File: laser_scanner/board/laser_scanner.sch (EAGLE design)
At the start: 31 parts

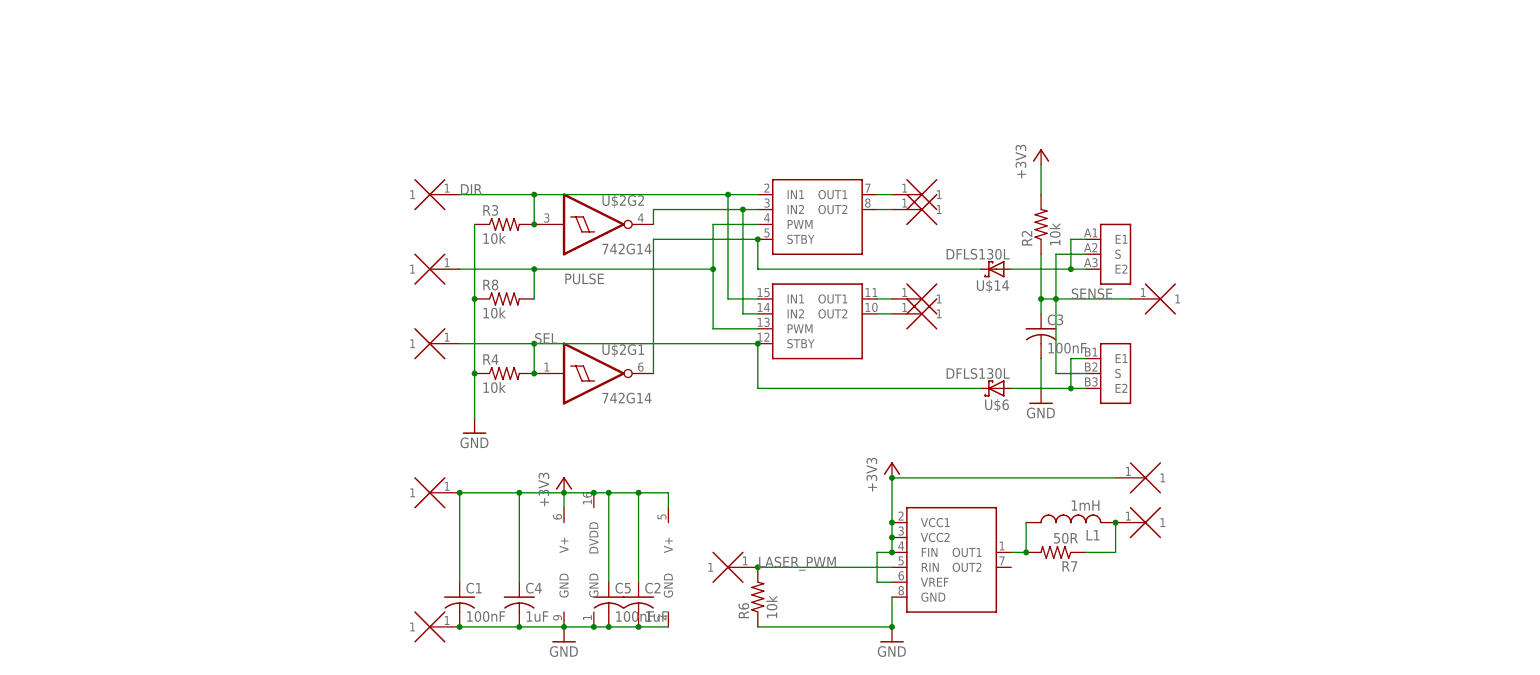
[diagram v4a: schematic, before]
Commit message: Made laser scanner more readable.
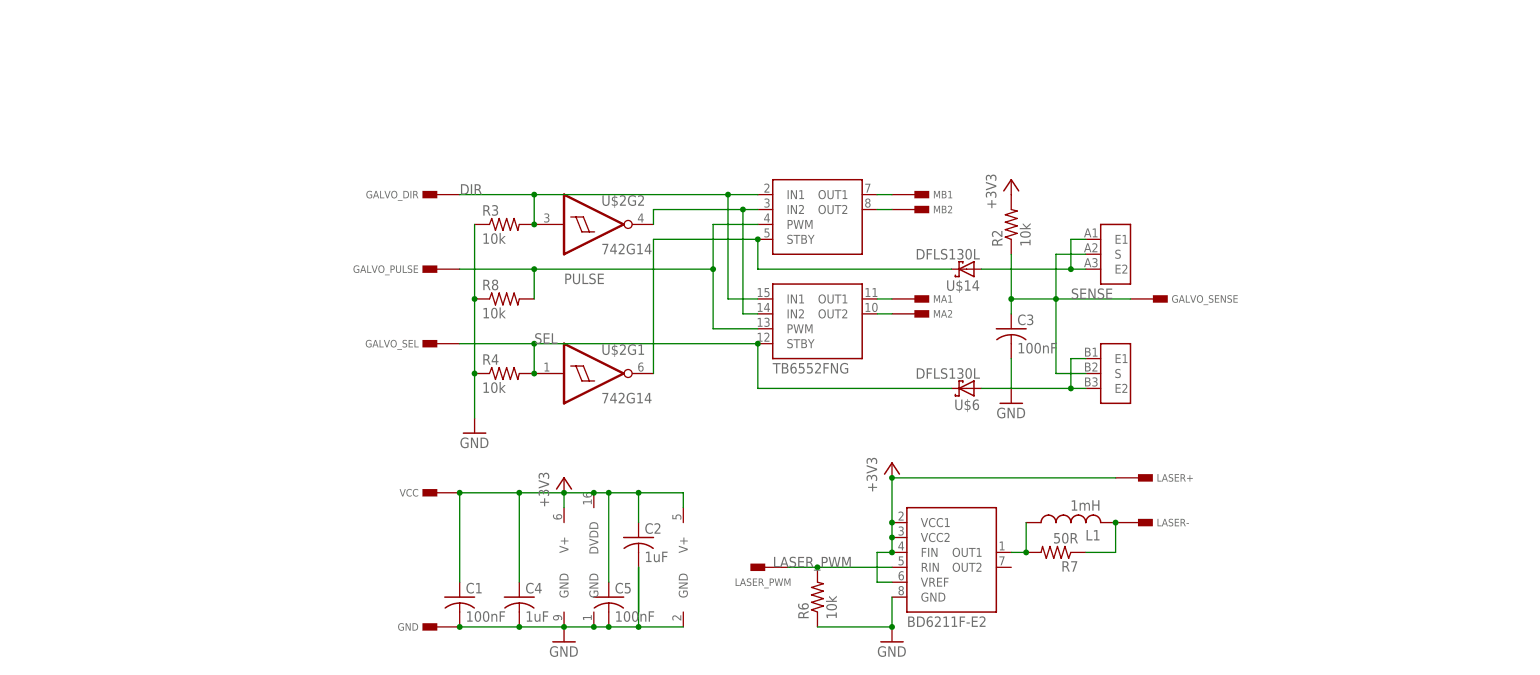
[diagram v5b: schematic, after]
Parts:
- renumbered L+ to LASER+, L- to LASER-
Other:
- note added: "BD6211F-E2"
- note added: "TB6552FNG"
- moved on the sheet: C2, C3, R2, R6, U$14, U$6
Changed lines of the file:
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@@
 <part name="R7" library="rcl" deviceset="R-US_" device="R0603" value="50R"/>
 <part name="LASER_PWM" library="modular_robotics" deviceset="PAD" device="-0.6_1.8"/>
-<part name="L-" library="modular_robotics" deviceset="PAD" device="-0.6_1.8"/>
+<part name="LASER-" library="modular_robotics" deviceset="PAD" device="-0.6_1.8"/>
 <part name="U$3" library="modular_robotics" deviceset="BD6211" device=""/>
 <part name="GND5" library="supply1" deviceset="GND" device=""/>
 <part name="+3V5" library="supply1" deviceset="+3V3" device=""/>
-<part name="L+" library="modular_robotics" deviceset="PAD" device="-0.6_1.8"/>
+<part name="LASER+" library="modular_robotics" deviceset="PAD" device="-0.6_1.8"/>
 <part name="R8" library="rcl" deviceset="R-US_" device="R0603" value="10k"/>
 <part name="U$2" library="modular_robotics" deviceset="74*2G14" device=""/>
@@
 <sheet>
 <plain>
+<text x="137.16" y="-15.24" size="1.778" layer="95">BD6211F-E2</text>
+<text x="114.3" y="27.94" size="1.778" layer="95">TB6552FNG</text>
 </plain>
 <instances>
@@
 <instance part="MA2" gate="G$1" x="139.7" y="38.1"/>
 <instance part="C1" gate="G$1" x="60.96" y="-10.16"/>
-<instance part="C2" gate="G$1" x="91.44" y="-10.16"/>
-<instance part="U$6" gate="G$1" x="152.4" y="25.4" rot="R180"/>
-<instance part="R2" gate="G$1" x="160.02" y="53.34" rot="R90"/>
+<instance part="C2" gate="G$1" x="91.44" y="0"/>
+<instance part="U$6" gate="G$1" x="147.32" y="25.4" rot="R180"/>
+<instance part="R2" gate="G$1" x="154.94" y="53.34" rot="R90"/>
 <instance part="U$7" gate="A" x="170.18" y="48.26"/>
 <instance part="U$7" gate="B" x="170.18" y="27.94"/>
@@
 <instance part="GND2" gate="1" x="63.5" y="17.78"/>
 <instance part="R4" gate="G$1" x="68.58" y="27.94"/>
-<instance part="C3" gate="G$1" x="160.02" y="35.56"/>
-<instance part="U$14" gate="G$1" x="152.4" y="45.72" rot="R180"/>
-<instance part="+3V3" gate="G$1" x="160.02" y="66.04"/>
-<instance part="GND3" gate="1" x="160.02" y="22.86"/>
+<instance part="C3" gate="G$1" x="154.94" y="35.56"/>
+<instance part="U$14" gate="G$1" x="147.32" y="45.72" rot="R180"/>
+<instance part="+3V3" gate="G$1" x="154.94" y="60.96"/>
+<instance part="GND3" gate="1" x="154.94" y="22.86"/>
 <instance part="L1" gate="G$1" x="165.1" y="2.54" rot="R90"/>
-<instance part="R6" gate="G$1" x="111.76" y="-10.16" rot="R90"/>
+<instance part="R6" gate="G$1" x="121.92" y="-10.16" rot="R90"/>
 <instance part="R7" gate="G$1" x="162.56" y="-2.54" rot="R180"/>
-<instance part="LASER_PWM" gate="G$1" x="106.68" y="-5.08" rot="R180"/>
-<instance part="L-" gate="G$1" x="177.8" y="2.54"/>
+<instance part="LASER_PWM" gate="G$1" x="111.76" y="-5.08" smashed="yes" rot="R180">
+<attribute name="NAME" x="117.475" y="-6.985" size="1.27" layer="95" rot="R180"/>
+</instance>
+<instance part="LASER-" gate="G$1" x="177.8" y="2.54"/>
 <instance part="U$3" gate="G$1" x="137.16" y="-12.7"/>
 <instance part="GND5" gate="1" x="134.62" y="-17.78"/>
 <instance part="+3V5" gate="G$1" x="134.62" y="12.7"/>
-<instance part="L+" gate="G$1" x="177.8" y="10.16"/>
+<instance part="LASER+" gate="G$1" x="177.8" y="10.16"/>
 <instance part="R8" gate="G$1" x="68.58" y="40.64"/>
-<instance part="U$2" gate="PWR" x="96.52" y="-5.08"/>
+<instance part="U$2" gate="PWR" x="99.06" y="-5.08"/>
 <instance part="U$2" gate="G2" x="83.82" y="53.34"/>
 <instance part="U$2" gate="G1" x="83.82" y="27.94"/>
@@
 <pinref part="U$2" gate="PWR" pin="GND"/>
 <wire x1="86.36" y1="-15.24" x2="91.44" y2="-15.24" width="0.1524" layer="91"/>
-<wire x1="96.52" y1="-15.24" x2="91.44" y2="-15.24" width="0.1524" layer="91"/>
-<junction x="91.44" y="-15.24"/>
+<wire x1="91.44" y1="-12.7" x2="91.44" y2="-5.08" width="0.1524" layer="91"/>
+<wire x1="99.06" y1="-15.24" x2="91.44" y2="-15.24" width="0.1524" layer="91"/>
+<wire x1="91.44" y1="-15.24" x2="91.44" y2="-5.08" width="0.1524" layer="91"/>
 <pinref part="C4" gate="G$1" pin="2"/>
 <junction x="71.12" y="-15.24"/>
 <pinref part="C5" gate="G$1" pin="2"/>
 <junction x="86.36" y="-15.24"/>
+<junction x="91.44" y="-15.24"/>
 </segment>
 <segment>
@@
 <pinref part="GND3" gate="1" pin="GND"/>
 <pinref part="C3" gate="G$1" pin="2"/>
-<wire x1="160.02" y1="25.4" x2="160.02" y2="30.48" width="0.1524" layer="91"/>
+<wire x1="154.94" y1="25.4" x2="154.94" y2="30.48" width="0.1524" layer="91"/>
 </segment>
 <segment>
@@
 <pinref part="U$3" gate="G$1" pin="GND"/>
 <pinref part="R6" gate="G$1" pin="1"/>
-<wire x1="134.62" y1="-15.24" x2="111.76" y2="-15.24" width="0.1524" layer="91"/>
+<wire x1="134.62" y1="-15.24" x2="121.92" y2="-15.24" width="0.1524" layer="91"/>
 <junction x="134.62" y="-15.24"/>
 <wire x1="134.62" y1="-10.16" x2="134.62" y2="-15.24" width="0.1524" layer="91"/>
@@
 <wire x1="60.96" y1="7.62" x2="60.96" y2="-7.62" width="0.1524" layer="91"/>
 <pinref part="C2" gate="G$1" pin="1"/>
-<wire x1="91.44" y1="-7.62" x2="91.44" y2="7.62" width="0.1524" layer="91"/>
+<wire x1="91.44" y1="2.54" x2="91.44" y2="7.62" width="0.1524" layer="91"/>
 <pinref part="U$1" gate="DPWR" pin="DVDD"/>
 <wire x1="91.44" y1="7.62" x2="86.36" y2="7.62" width="0.1524" layer="91"/>
@@
 <junction x="60.96" y="7.62"/>
 <pinref part="U$2" gate="PWR" pin="V+"/>
-<wire x1="96.52" y1="5.08" x2="96.52" y2="7.62" width="0.1524" layer="91"/>
-<wire x1="96.52" y1="7.62" x2="91.44" y2="7.62" width="0.1524" layer="91"/>
+<wire x1="99.06" y1="5.08" x2="99.06" y2="7.62" width="0.1524" layer="91"/>
+<wire x1="99.06" y1="7.62" x2="91.44" y2="7.62" width="0.1524" layer="91"/>
 <junction x="91.44" y="7.62"/>
 <pinref part="C4" gate="G$1" pin="1"/>
@@
 <pinref part="R2" gate="G$1" pin="2"/>
 <pinref part="+3V3" gate="G$1" pin="+3V3"/>
-<wire x1="160.02" y1="58.42" x2="160.02" y2="63.5" width="0.1524" layer="91"/>
-</segment>
-<segment>
-<pinref part="L+" gate="G$1" pin="1"/>
+</segment>
+<segment>
+<pinref part="LASER+" gate="G$1" pin="1"/>
 <wire x1="172.72" y1="10.16" x2="134.62" y2="10.16" width="0.1524" layer="91"/>
 <pinref part="U$3" gate="G$1" pin="VCC2"/>
@@
 <wire x1="60.96" y1="33.02" x2="73.66" y2="33.02" width="0.1524" layer="91"/>
 <wire x1="73.66" y1="33.02" x2="111.76" y2="33.02" width="0.1524" layer="91"/>
-<wire x1="149.86" y1="25.4" x2="111.76" y2="25.4" width="0.1524" layer="91"/>
+<wire x1="144.78" y1="25.4" x2="111.76" y2="25.4" width="0.1524" layer="91"/>
 <wire x1="111.76" y1="25.4" x2="111.76" y2="33.02" width="0.1524" layer="91"/>
 <junction x="111.76" y="33.02"/>
@@
 <pinref part="U$14" gate="G$1" pin="A"/>
 <pinref part="U$7" gate="A" pin="E2"/>
-<wire x1="154.94" y1="45.72" x2="165.1" y2="45.72" width="0.1524" layer="91"/>
+<wire x1="149.86" y1="45.72" x2="165.1" y2="45.72" width="0.1524" layer="91"/>
 <pinref part="U$7" gate="A" pin="E1"/>
 <wire x1="165.1" y1="45.72" x2="167.64" y2="45.72" width="0.1524" layer="91"/>
@@
 <wire x1="165.1" y1="25.4" x2="167.64" y2="25.4" width="0.1524" layer="91"/>
 <pinref part="U$6" gate="G$1" pin="A"/>
-<wire x1="165.1" y1="25.4" x2="154.94" y2="25.4" width="0.1524" layer="91"/>
+<wire x1="165.1" y1="25.4" x2="149.86" y2="25.4" width="0.1524" layer="91"/>
 <junction x="165.1" y="25.4"/>
 </segment>
@@
 <pinref part="C3" gate="G$1" pin="1"/>
 <pinref part="R2" gate="G$1" pin="1"/>
-<wire x1="160.02" y1="38.1" x2="160.02" y2="40.64" width="0.1524" layer="91"/>
-<wire x1="160.02" y1="40.64" x2="160.02" y2="48.26" width="0.1524" layer="91"/>
-<wire x1="162.56" y1="40.64" x2="160.02" y2="40.64" width="0.1524" layer="91"/>
-<junction x="160.02" y="40.64"/>
+<wire x1="154.94" y1="38.1" x2="154.94" y2="40.64" width="0.1524" layer="91"/>
+<wire x1="154.94" y1="40.64" x2="154.94" y2="48.26" width="0.1524" layer="91"/>
+<wire x1="162.56" y1="40.64" x2="154.94" y2="40.64" width="0.1524" layer="91"/>
+<junction x="154.94" y="40.64"/>
 <label x="165.1" y="40.64" size="1.778" layer="95"/>
 </segment>
@@
 <pinref part="LASER_PWM" gate="G$1" pin="1"/>
 <pinref part="LASER_PWM" gate="G$1" pin="1"/>
-<junction x="111.76" y="-5.08"/>
+<junction x="121.92" y="-5.08"/>
 <pinref part="U$3" gate="G$1" pin="RIN"/>
-<wire x1="134.62" y1="-5.08" x2="111.76" y2="-5.08" width="0.1524" layer="91"/>
-<label x="111.76" y="-5.08" size="1.778" layer="95"/>
+<wire x1="134.62" y1="-5.08" x2="121.92" y2="-5.08" width="0.1524" layer="91"/>
+<label x="114.3" y="-5.08" size="1.778" layer="95"/>
+<wire x1="121.92" y1="-5.08" x2="116.84" y2="-5.08" width="0.1524" layer="91"/>
 </segment>
 </net>
@@
 <pinref part="L1" gate="G$1" pin="2"/>
 <wire x1="172.72" y1="-2.54" x2="172.72" y2="2.54" width="0.1524" layer="91"/>
-<pinref part="L-" gate="G$1" pin="1"/>
+<pinref part="LASER-" gate="G$1" pin="1"/>
 <junction x="172.72" y="2.54"/>
 </segment>
@@
 <wire x1="93.98" y1="50.8" x2="111.76" y2="50.8" width="0.1524" layer="91"/>
 <wire x1="93.98" y1="27.94" x2="93.98" y2="50.8" width="0.1524" layer="91"/>
-<wire x1="149.86" y1="45.72" x2="111.76" y2="45.72" width="0.1524" layer="91"/>
+<wire x1="144.78" y1="45.72" x2="111.76" y2="45.72" width="0.1524" layer="91"/>
 <wire x1="111.76" y1="45.72" x2="111.76" y2="50.8" width="0.1524" layer="91"/>
 <junction x="111.76" y="50.8"/>
